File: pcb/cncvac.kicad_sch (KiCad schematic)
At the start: 36 parts, among them J1 AVR-ISP-6, J2 TRIG, SW1 SW_SPST, U1 ATtiny841-SS, U2 MICRF112YMM, U3 LTV-357T, Y1 13.56MHz, Y2 8MHz

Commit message: tweak
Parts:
- added J3: U.FL, Connector_Coaxial:U.FL_Hirose_U.FL-R-SMT-1_Vertical, symbol Connector:Conn_Coaxial
- added R6, R7: 0, Resistor_SMD:R_0402_1005Metric, symbol Device:R_Small
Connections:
- net GND: now also J3.2 (Ext)
- net at C7.1, L2.2: now also R6.2, R7.1; no longer AE1.2
- new net: AE1.2, R6.1
- new net: J3.1 (In), R7.2
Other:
- moved on the sheet: AE1, J1

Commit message: pn's
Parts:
- U1: LCSC (none) -> C614879
- U2: LCSC (none) -> C481379
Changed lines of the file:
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@@
 			)
 		)
-		(property "LCSC" ""
+		(property "LCSC" "C481379"
 			(at 75.8541 113.03 0)
 			(effects
@@
 			)
 		)
-		(property "LCSC" ""
+		(property "LCSC" "C614879"
 			(at 114.8334 52.1716 0)
 			(effects

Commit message: shift the antenna opening in the panel slightly
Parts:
- R4, R5: value 1k -> 22k; footprint Resistor_SMD:R_0402_1005Metric -> Resistor_SMD:R_0805_2012Metric; LCSC C11702 -> C17560
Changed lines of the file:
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@@
 			)
 		)
-		(property "Value" "1k"
+		(property "Value" "22k"
 			(at 63.5 68.58 90)
 			(effects
@@
 			)
 		)
-		(property "Footprint" "Resistor_SMD:R_0402_1005Metric"
+		(property "Footprint" "Resistor_SMD:R_0805_2012Metric"
 			(at 63.5 71.12 0)
 			(effects
@@
 			)
 		)
-		(property "LCSC" "C11702"
+		(property "LCSC" "C17560"
 			(at 62.3316 69.6214 0)
 			(effects
@@
 			)
 		)
-		(property "Value" "1k"
+		(property "Value" "22k"
 			(at 58.42 62.23 90)
 			(effects
@@
 			)
 		)
-		(property "Footprint" "Resistor_SMD:R_0402_1005Metric"
+		(property "Footprint" "Resistor_SMD:R_0805_2012Metric"
 			(at 58.42 64.77 0)
 			(effects
@@
 			)
 		)
-		(property "LCSC" "C11702"
+		(property "LCSC" "C17560"
 			(at 57.2516 63.2714 0)
 			(effects

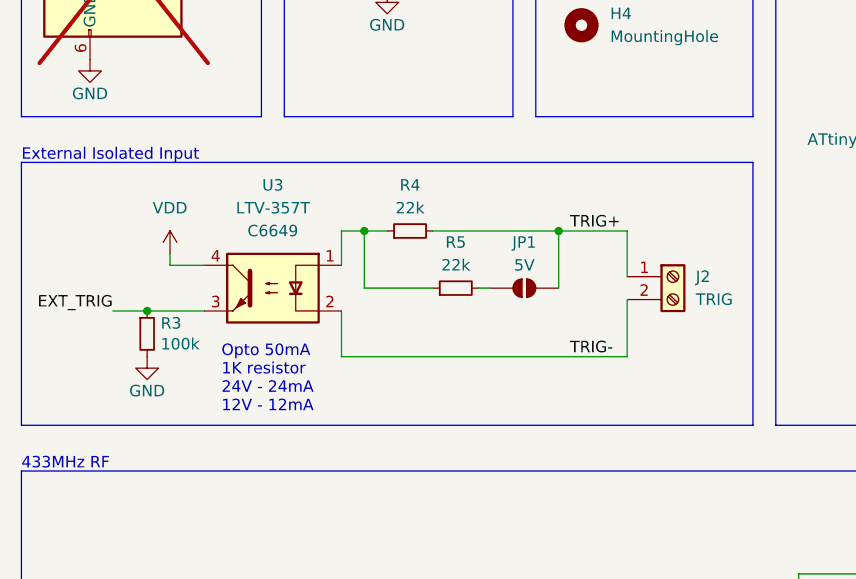
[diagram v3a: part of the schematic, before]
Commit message: Add protection diode to opto, increase pulldown strength
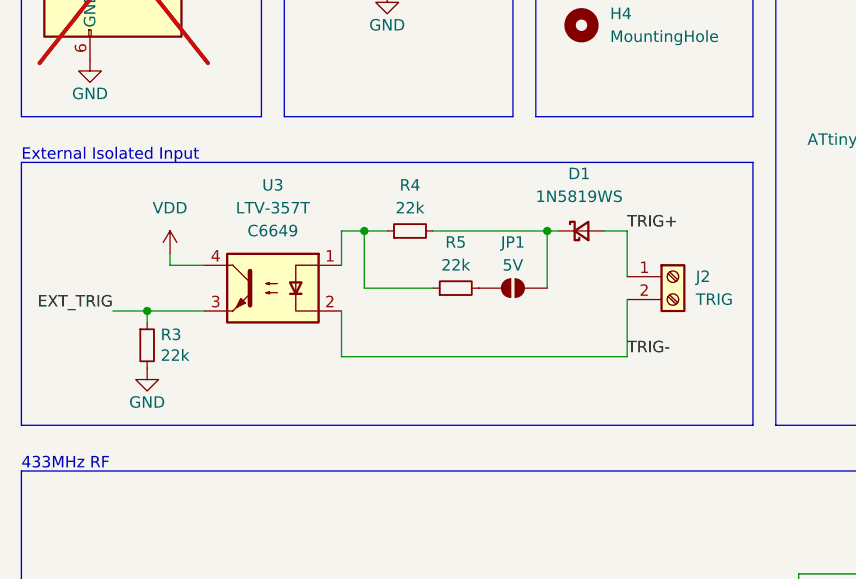
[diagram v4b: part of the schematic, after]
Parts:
- added D1: 1N5819WS, Diode_SMD:D_SOD-323, symbol Device:D_Schottky_Small
- R3: value 100k -> 22k; footprint Resistor_SMD:R_0402_1005Metric -> Resistor_SMD:R_0805_2012Metric; LCSC C25741 -> C17560
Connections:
- net TRIG+: now also D1.2 (A); no longer JP1.2 (B), R4.2
- new net: D1.1 (K), JP1.2 (B), R4.2
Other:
- note removed: "Opto 50mA 1K resistor 24V - 24mA 12V - 12mA"
- moved on the sheet: JP1, R3
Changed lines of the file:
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@@
 	)
 	(junction
-		(at 74.93 64.77)
-		(diameter 0)
-		(color 0 0 0 0)
-	)
-	(junction
 		(at 109.22 102.87)
 		(diameter 0)
@@
 	)
 	(junction
+		(at 73.66 64.77)
+		(diameter 0)
+		(color 0 0 0 0)
+	)
+	(junction
 		(at 101.6 128.27)
 		(diameter 0)
@@
 	(wire
 		(pts
+			(xy 80.01 64.77) (xy 82.55 64.77)
+		)
+		(stroke
+			(width 0)
+			(type default)
+		)
+	)
+	(wire
+		(pts
 			(xy 50.8 78.74) (xy 50.8 73.66)
 		)
@@
 	(wire
 		(pts
-			(xy 66.04 71.12) (xy 67.31 71.12)
-		)
-		(stroke
-			(width 0)
-			(type default)
-		)
-	)
-	(wire
-		(pts
 			(xy 120.65 128.27) (xy 114.3 128.27)
 		)
@@
 	(wire
 		(pts
-			(xy 74.93 64.77) (xy 74.93 71.12)
+			(xy 73.66 64.77) (xy 73.66 71.12)
 		)
 		(stroke
@@
 	(wire
 		(pts
+			(xy 73.66 64.77) (xy 74.93 64.77)
+		)
+		(stroke
+			(width 0)
+			(type default)
+		)
+	)
+	(wire
+		(pts
 			(xy 147.32 80.01) (xy 154.94 80.01)
 		)
@@
 	(wire
 		(pts
+			(xy 29.21 74.93) (xy 29.21 73.66)
+		)
+		(stroke
+			(width 0)
+			(type default)
+		)
+	)
+	(wire
+		(pts
 			(xy 146.05 50.8) (xy 143.51 50.8)
 		)
@@
 	(wire
 		(pts
-			(xy 60.96 64.77) (xy 74.93 64.77)
+			(xy 60.96 64.77) (xy 73.66 64.77)
 		)
 		(stroke
@@
 		)
 	)
-	(wire
-		(pts
-			(xy 74.93 64.77) (xy 82.55 64.77)
-		)
-		(stroke
-			(width 0)
-			(type default)
-		)
-	)
 	(rectangle
 		(start 72.39 15.24)
@@
 		)
 	)
-	(text "Opto 50mA\n1K resistor\n24V - 24mA\n12V - 12mA"
-		(exclude_from_sim no)
-		(at 37.465 85.09 0)
-		(effects
-			(font
-				(size 1.27 1.27)
-			)
-			(justify left bottom)
-		)
-	)
 	(text "Programming"
 		(exclude_from_sim no)
@@
 	(label "MOSI"
 		(at 146.05 53.34 0)
-		(fields_autoplaced yes)
 		(effects
 			(font
@@
 	)
 	(label "TRIG+"
-		(at 76.2 64.77 0)
-		(fields_autoplaced yes)
+		(at 82.55 64.77 0)
 		(effects
 			(font
@@
 	(label "EXT_TRIG"
 		(at 25.4 73.66 180)
-		(fields_autoplaced yes)
 		(effects
 			(font
@@
 	(label "SCK"
 		(at 146.05 48.26 0)
-		(fields_autoplaced yes)
 		(effects
 			(font
@@
 	(label "EN"
 		(at 93.98 120.65 180)
-		(fields_autoplaced yes)
 		(effects
 			(font
@@
 	(label "RST"
 		(at 143.51 68.58 0)
-		(fields_autoplaced yes)
 		(effects
 			(font
@@
 	(label "RST"
 		(at 35.56 38.1 0)
-		(fields_autoplaced yes)
 		(effects
 			(font
@@
 	(label "EXT_TRIG"
 		(at 146.05 45.72 0)
-		(fields_autoplaced yes)
 		(effects
 			(font
@@
 	(label "EN"
 		(at 146.05 38.1 0)
-		(fields_autoplaced yes)
 		(effects
 			(font
@@
 	(label "ASK"
 		(at 58.42 123.19 0)
-		(fields_autoplaced yes)
 		(effects
 			(font
@@
 	(label "FSK"
 		(at 146.05 40.64 0)
-		(fields_autoplaced yes)
 		(effects
 			(font
@@
 	(label "MISO"
 		(at 35.56 30.48 0)
-		(fields_autoplaced yes)
 		(effects
 			(font
@@
 	(label "ASK"
 		(at 146.05 43.18 0)
-		(fields_autoplaced yes)
 		(effects
 			(font
@@
 	(label "SCK"
 		(at 35.56 35.56 0)
-		(fields_autoplaced yes)
 		(effects
 			(font
@@
 	)
 	(label "TRIG-"
-		(at 76.2 78.74 0)
-		(fields_autoplaced yes)
+		(at 82.55 78.74 0)
 		(effects
 			(font
@@
 	(label "MISO"
 		(at 146.05 50.8 0)
-		(fields_autoplaced yes)
 		(effects
 			(font
@@
 	(label "FSK"
 		(at 58.42 120.65 0)
-		(fields_autoplaced yes)
 		(effects
 			(font
@@
 	(label "MOSI"
 		(at 35.56 33.02 0)
-		(fields_autoplaced yes)
 		(effects
 			(font
@@
 	(symbol
 		(lib_id "power:GND")
-		(at 29.21 78.74 0)
+		(at 29.21 80.01 0)
 		(unit 1)
 		(exclude_from_sim no)
@@
 		(dnp no)
 		(property "Reference" "#PWR021"
-			(at 29.21 85.09 0)
+			(at 29.21 86.36 0)
 			(effects
 				(font
@@
 		)
 		(property "Value" "GND"
-			(at 29.21 82.55 0)
+			(at 29.21 83.82 0)
 			(effects
 				(font
@@
 		)
 		(property "Footprint" ""
-			(at 29.21 78.74 0)
+			(at 29.21 80.01 0)
 			(effects
 				(font
@@
 		)
 		(property "Datasheet" ""
-			(at 29.21 78.74 0)
+			(at 29.21 80.01 0)
 			(effects
 				(font
@@
 		)
 		(property "Description" "Power symbol creates a global label with name \"GND\" , ground"
-			(at 29.21 78.74 0)
+			(at 29.21 80.01 0)
 			(effects
 				(font
@@
 	(symbol
 		(lib_id "Jumper:SolderJumper_2_Open")
-		(at 71.12 71.12 0)
+		(at 69.85 71.12 0)
 		(unit 1)
 		(exclude_from_sim yes)
@@
 		(dnp no)
 		(property "Reference" "JP1"
-			(at 71.12 66.04 0)
+			(at 69.85 66.04 0)
 			(effects
 				(font
@@
 		)
 		(property "Value" "5V"
-			(at 71.12 68.58 0)
+			(at 69.85 68.58 0)
 			(effects
 				(font
@@
 		)
 		(property "Footprint" "Jumper:SolderJumper-2_P1.3mm_Open_RoundedPad1.0x1.5mm"
-			(at 71.12 71.12 0)
+			(at 69.85 71.12 0)
 			(effects
 				(font
@@
 		)
 		(property "Datasheet" "~"
-			(at 71.12 71.12 0)
+			(at 69.85 71.12 0)
 			(effects
 				(font
@@
 		)
 		(property "Description" "Solder Jumper, 2-pole, open"
-			(at 71.12 71.12 0)
+			(at 69.85 71.12 0)
 			(effects
 				(font
@@
 	(symbol
 		(lib_id "Device:R_Small")
-		(at 29.21 76.2 0)
+		(at 29.21 77.47 0)
 		(unit 1)
 		(exclude_from_sim no)
@@
 		(dnp no)
 		(property "Reference" "R3"
-			(at 30.7086 75.0316 0)
+			(at 30.7086 76.3016 0)
 			(effects
 				(font
@@
 			)
 		)
-		(property "Value" "100k"
-			(at 30.7086 77.343 0)
+		(property "Value" "22k"
+			(at 30.7086 78.613 0)
 			(effects
 				(font
@@
 			)
 		)
-		(property "Footprint" "Resistor_SMD:R_0402_1005Metric"
-			(at 29.21 76.2 0)
+		(property "Footprint" "Resistor_SMD:R_0805_2012Metric"
+			(at 29.21 77.47 0)
 			(effects
 				(font
@@
 		)
 		(property "Datasheet" "~"
-			(at 29.21 76.2 0)
+			(at 29.21 77.47 0)
 			(effects
 				(font
@@
 		)
 		(property "Description" "Resistor, small symbol"
-			(at 29.21 76.2 0)
+			(at 29.21 77.47 0)
 			(effects
 				(font
@@
 			)
 		)
-		(property "LCSC" "C25741"
-			(at 30.7086 75.0316 0)
+		(property "LCSC" "C17560"
+			(at 30.7086 76.3016 0)
 			(effects
 				(font
@@
 			)
 		)
+		(property "Notes" ""
+			(at 29.21 77.47 0)
+			(effects
+				(font
+					(size 1.27 1.27)
+				)
+			)
+		)
 		(pin "1"
 		)
@@
 					(unit 1)
 				)
+			)
+		)
+	)
+	(symbol
+		(lib_id "Device:D_Schottky_Small")
+		(at 77.47 64.77 0)
+		(unit 1)
+		(exclude_from_sim no)
+		(in_bom yes)
+		(on_board yes)
+		(dnp no)
+		(fields_autoplaced yes)
+		(property "Reference" "D1"
+			(at 77.216 58.42 0)
+			(effects
+				(font
+					(size 1.27 1.27)
+				)
+			)
+		)
+		(property "Value" "1N5819WS"
+			(at 77.216 60.96 0)
+			(effects
+				(font
+					(size 1.27 1.27)
+				)
+			)
+		)
+		(property "Footprint" "Diode_SMD:D_SOD-323"
+			(at 77.47 64.77 90)
+			(effects
+				(font
+					(size 1.27 1.27)
+				)
+				(hide yes)
+			)
+		)
+		(property "Datasheet" "~"
+			(at 77.47 64.77 90)
+			(effects
+				(font
+					(size 1.27 1.27)
+				)
+				(hide yes)
+			)
+		)
+		(property "Description" "Schottky diode, small symbol"
+			(at 77.47 64.77 0)
+			(effects
+				(font
+					(size 1.27 1.27)
+				)
+				(hide yes)
+			)
+		)
+		(property "LCSC" "C191023"
+			(at 77.47 64.77 0)
+			(effects
+				(font
+					(size 1.27 1.27)
+				)
+				(hide yes)
+			)
+		)
+		(property "Notes" ""
+			(at 77.47 64.77 0)
+			(effects
+				(font
+					(size 1.27 1.27)
+				)
+				(hide yes)
+			)
+		)
+		(pin "1"
+		)
+		(pin "2"
+		)
+		(instances
+			(project ""
+				(path "/01863d9d-9fc2-4c77-932b-012f900a4f45"
+					(reference "D1")
+					(unit 1)
+				)

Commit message: fixup
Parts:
- added JP2: SolderJumper_3_Bridged12, Jumper:SolderJumper-3_P1.3mm_Bridged12_RoundedPad1.0x1.5mm_NumberLabels, symbol Jumper:SolderJumper_3_Bridged12
- added R10, R11, R12, R8, R9: 100k, Resistor_SMD:R_0402_1005Metric, symbol Device:R_Small
- added SW2: SW_DIP_x05, Button_Switch_THT:SW_DIP_SPSTx05_Slide_9.78x14.88mm_W7.62mm_P2.54mm, symbol Switch:SW_DIP_x05
- R7: now left out of the parts list
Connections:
- net ASK: now also JP2.1 (A); no longer U1.11 (PA2)
- net EXT_TRIG: now also U1.11 (PA2); no longer U1.10 (PA3)
- net FSK: now also JP2.3 (B); no longer U1.12 (PA1)
- net GND: now also R10.2, R11.2, R12.2, R8.2, R9.2
- net DIP4: now reaches U1.5 (PB2)
- net DIP4: now also SW2.7
- net MISO renamed DIP2
- net DIP2: now also SW2.9
- net MOSI renamed DIP5
- net DIP5: now also SW2.6
- net SCK renamed DIP3
- net DIP3: now also SW2.8
- new net: R8.1, SW2.1
- new net: R10.1, SW2.2
- new net: R12.1, SW2.3
- new net: R9.1, SW2.4
- new net: R11.1, SW2.5
- new net DATA: JP2.2 (C), U1.12 (PA1)
- new net DIP1: SW2.10, U1.10 (PA3)
- no-connect marks 2 -> 1
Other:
- note added: "10pF gives 33.5kHz spread Only req'd for FSK, but ASK still works"
- note added: "DIP Switches"
- note removed: "10pF gives 33.5kHz spread"
- title: TPMS Silencer -> CNC Vac
- moved on the sheet: J2, SW1

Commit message: update part number for opto
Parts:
- U3: value LTV-357T -> EL357N; LCSC C6649 -> C42381015
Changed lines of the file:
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@@
 			)
 		)
-		(property "Value" "LTV-357T"
+		(property "Value" "EL357N"
 			(at 43.18 62.23 0)
 			(effects
@@
 			)
 		)
-		(property "LCSC" "C6649"
+		(property "LCSC" "C42381015"
 			(at 43.18 64.77 0)
 			(effects

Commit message: fix pn for opto
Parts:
- AE1: now not fitted; now left out of the parts list
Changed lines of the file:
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@@
 		(unit 1)
 		(exclude_from_sim no)
-		(in_bom yes)
+		(in_bom no)
 		(on_board yes)
-		(dnp no)
+		(dnp yes)
 		(property "Reference" "AE1"
 			(at 155.575 112.395 0)
@@
 					(size 1.27 1.27)
 				)
+				(hide yes)
 			)
 		)
@@
 					(size 1.27 1.27)
 				)
+				(hide yes)
 			)
 		)
